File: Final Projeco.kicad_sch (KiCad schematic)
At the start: 25 parts, among them SW1 SW_Omron_B3FS, SW2 SW_Omron_B3FS, U1 ESP32-S3, U2 GT-USB-7004N, U3 NCP167BMX330TBG, U4 LY68L6400SLIT, X1 TZ1269D

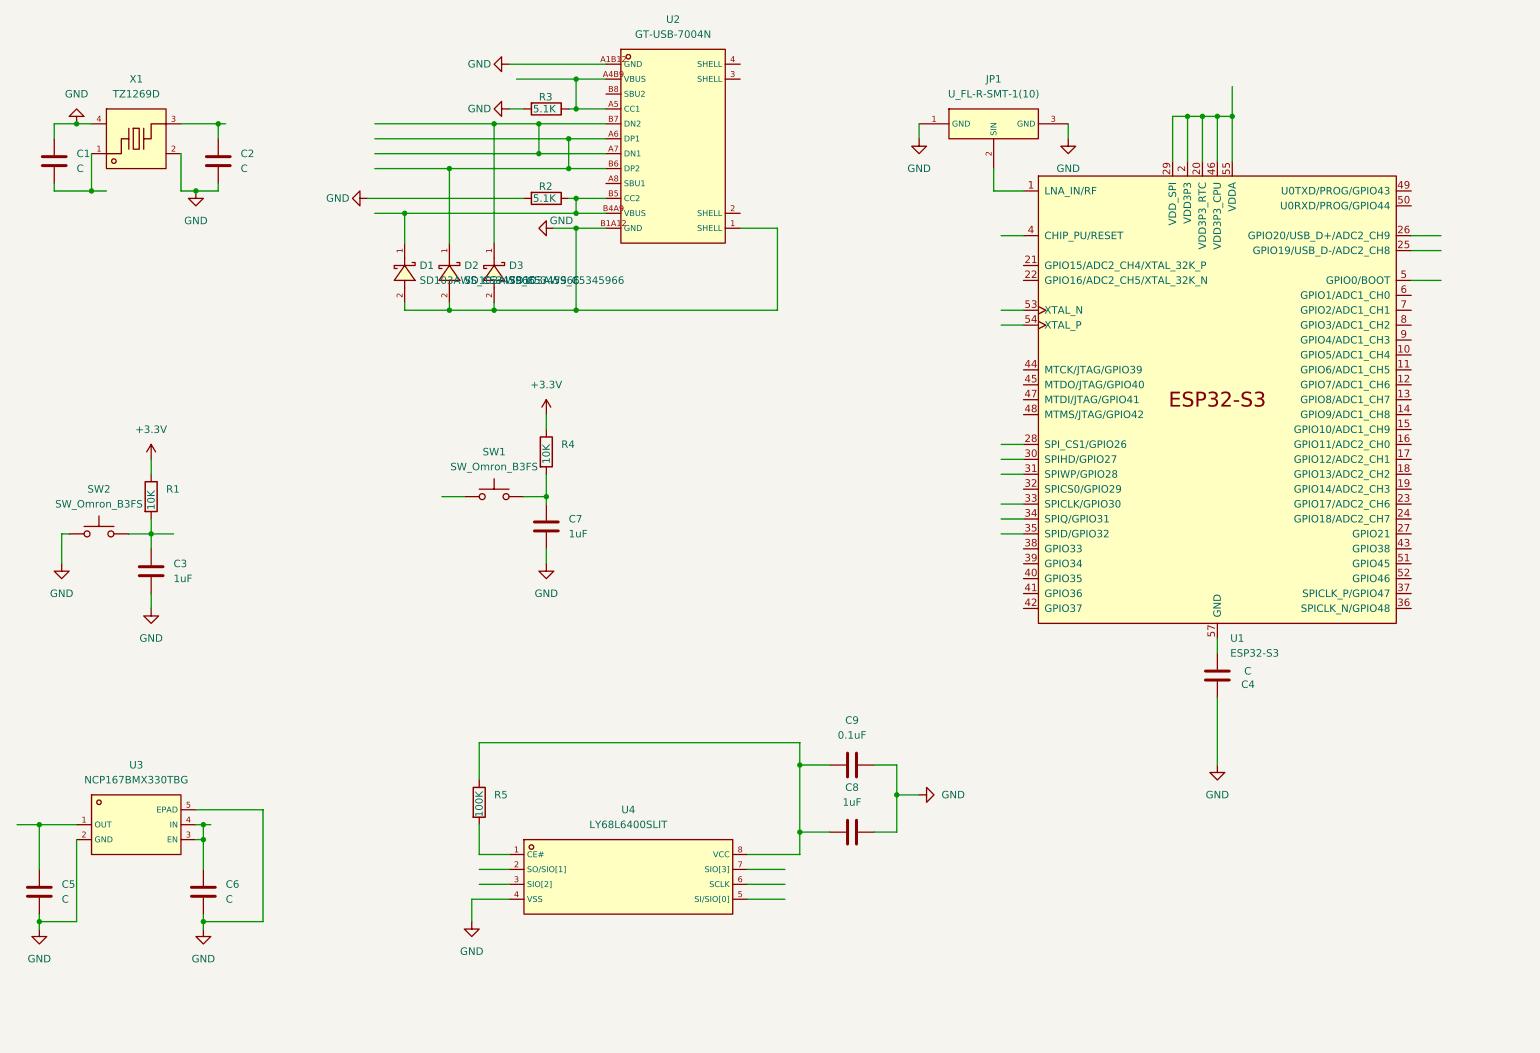
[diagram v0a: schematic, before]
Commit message: -Added some Headers
-Added Headers
-TODO (chore) (top priority):
 -    relabel EVERYTHING with net class (line) NOT directive (circle)
 -    get layout fixed
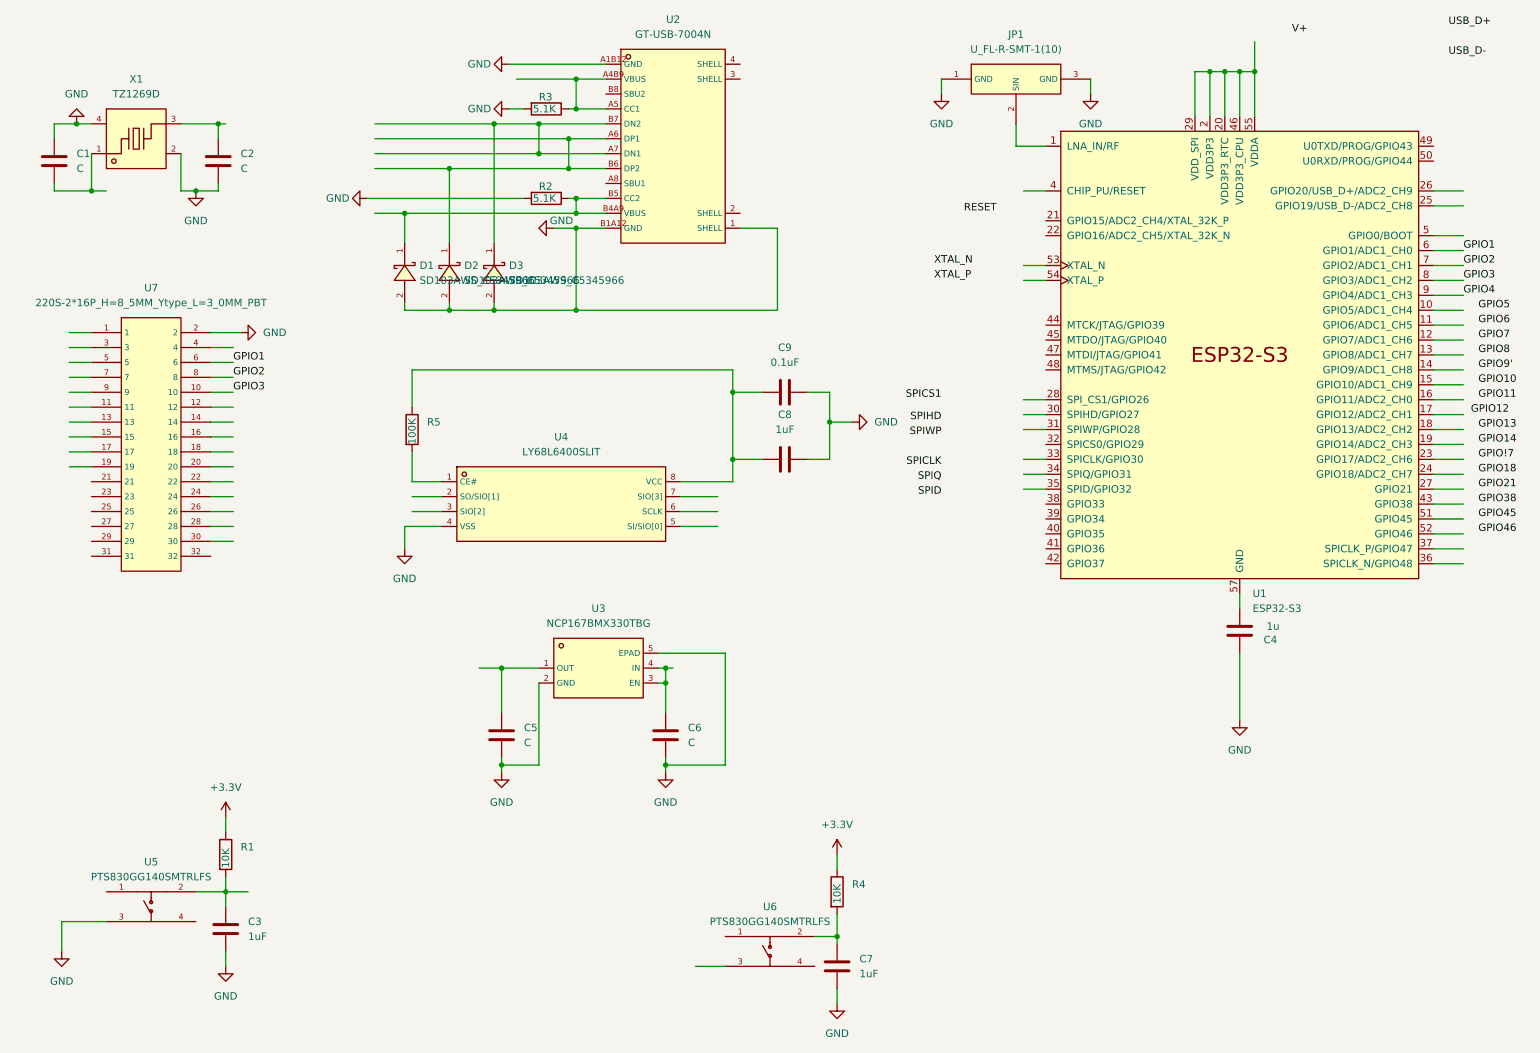
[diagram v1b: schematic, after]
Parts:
- removed SW1, SW2: SW_Omron_B3FS, symbol Switch:SW_Omron_B3FS
- added U5, U6: PTS830GG140SMTRLFS, jlc:KEY-SMD_4P-L3.1-W2.6_PTS830GG140SMTRLFS, symbol jlc:PTS830GG140SMTRLFS
- added U7: 220S-2*16P_H=8_5MM_Ytype_L=3_0MM_PBT, jlc:HDR-TH_32P-P2.54-V-F-R2-C16-S2.54, symbol LC:220S-2*16P_H=8_5MM_Ytype_L=3_0MM_PBT
- C4: value C -> 1u
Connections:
- net GND: now also U5.3, U7.2
- net GPIO1: now reaches U1.6 (GPIO1/ADC1_CH0)
- net GPIO1: now also U7.6
- net GPIO2: now reaches U1.7 (GPIO2/ADC1_CH1)
- net GPIO2: now also U7.8
- net GPIO3: now reaches U1.8 (GPIO3/ADC1_CH2)
- net GPIO3: now also U7.10
- net GPIO4: now reaches U1.9 (GPIO4/ADC1_CH3)
- net at C3.1, R1.2: now also U5.2
- net at C7.1, R4.2: now also U6.2
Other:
- moved on the sheet: C3, C4, C5, C6, C7, C8, C9, JP1, R1, R4, R5, U1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
